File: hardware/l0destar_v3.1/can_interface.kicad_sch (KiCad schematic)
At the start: 17 parts

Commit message: update v3.1
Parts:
- removed S9J1: CAN termination jumper, Connector_PinHeader_2.54mm:PinHeader_1x02_P2.54mm_Vertical, symbol Connector:Conn_01x02_Pin
- added J1: Conn_01x02_Pin, libs:PinHeader_1x02_P2.54mm_Vertical_Tight, symbol Connector:Conn_01x02_Pin
- added S9FL1: ACT1210-101-2P-TL00, libs:ACT12101012PTL00_tight, symbol ACT1210-101-2P-TL00:ACT1210-101-2P-TL00
- S9C5: value 0603 10uF 10V 20% X7T -> 0603 10uF 10V 20% X7R
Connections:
- net CAN_H: now also S9FL1.2; no longer S9U1.7 (CANH)
- net CAN_L: now also J1.2 (Pin_2), S9FL1.3; no longer S9U1.6 (CANL)
- net at S9R3.1: now also J1.1 (Pin_1)
- new net: S9FL1.4, S9U1.6 (CANL)
- new net: S9FL1.1, S9U1.7 (CANH)
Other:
- note added: "CAN termination resistor"
- moved on the sheet: S9D1, S9R1, S9R5, S9R7

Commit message: update v3.1
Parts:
- S9C1, S9C4: Manufacturer_Name (none) -> Multicomp Pro; Manufacturer_Part_Number (none) -> MC0402B104K250CT
- S9C2, S9C3: Manufacturer_Name (none) -> Murata; Manufacturer_Part_Number (none) -> GCM1555C1H270FA16D
- S9C5: Manufacturer_Name (none) -> TDK; Manufacturer_Part_Number (none) -> C1608X7R1A106M080AT
- S9D1: Manufacturer_Name (none) -> Diotec; Manufacturer_Part_Number (none) -> NUP2105L
- S9R1, S9R2, S9R4: Manufacturer_Name (none) -> Vishay; Manufacturer_Part_Number (none) -> CRCW040210K0FKED
- S9R3: Manufacturer_Name (none) -> Multicomp Pro; Manufacturer_Part_Number (none) -> MCPAS05W2J0121T5E
- S9R5: Manufacturer_Name (none) -> Vishay; Manufacturer_Part_Number (none) -> CRCW04021K00FKED
- S9R6, S9R7: Manufacturer_Name (none) -> Multicomp; Manufacturer_Part_Number (none) -> MC00625W04021220R
- S9U2: Manufacturer_Name (none) -> Microchip; Manufacturer_Part_Number (none) -> MCP2518FD
- S9Y1: Manufacturer_Name ECS -> ECS Inc

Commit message: 3.1 updates
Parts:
- renumbered J1 to S9J1
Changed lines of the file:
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@@
 		(dnp no)
 		(fields_autoplaced yes)
-		(property "Reference" "J1"
+		(property "Reference" "S9J1"
 			(at 153.67 34.29 0)
 			(show_name no)
@@
 			(project "l0destar"
 				(path "/d9f8328e-d6fd-4b6c-867a-ed589e52ed08"
-					(reference "J1")
+					(reference "S9J1")
 					(unit 1)
 				)

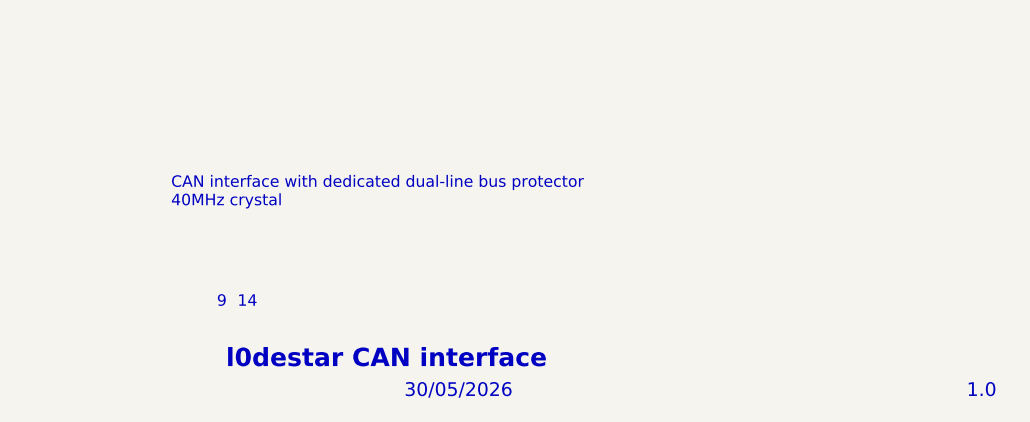
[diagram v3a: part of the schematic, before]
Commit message: update sheet annotations
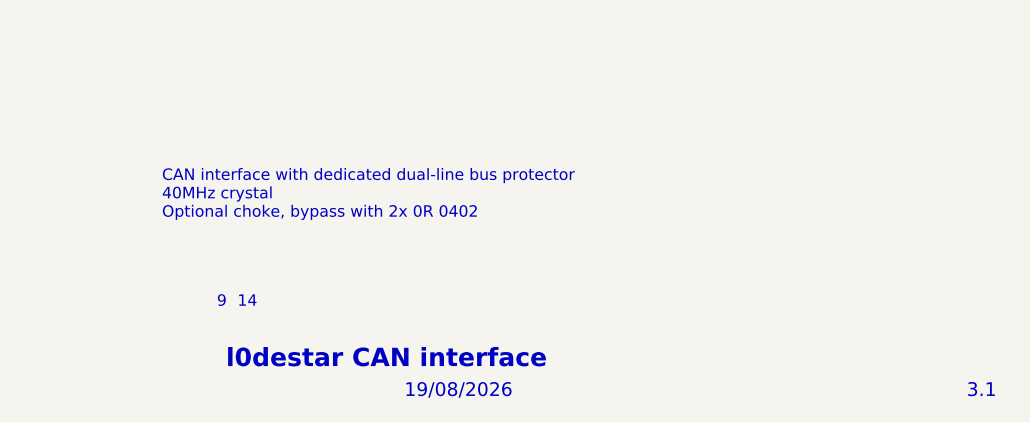
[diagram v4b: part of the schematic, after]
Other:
- note added: "19/08/2026"
- note added: "3.1"
- note added: "CAN interface with dedicated dual-line bus protector 40MHz crystal Optional choke, bypass with 2x 0R 0402"
- note removed: "1.0"
- note removed: "30/05/2026"
- note removed: "CAN interface with dedicated dual-line bus protector 40MHz crystal"
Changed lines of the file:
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@@
 	(generator_version "10.0")
 	(paper "A4")
-	(text "30/05/2026"
+	(text "19/08/2026"
 		(exclude_from_sim no)
 		(at 205.994 193.294 0)
@@
 		)
 	)
-	(text "CAN interface with dedicated dual-line bus protector\n40MHz crystal"
+	(text "CAN interface with dedicated dual-line bus protector\n40MHz crystal\nOptional choke, bypass with 2x 0R 0402"
 		(exclude_from_sim no)
-		(at 180.086 171.196 0)
+		(at 179.07 171.45 0)
 		(effects
 			(font
@@
 		)
 	)
-	(text "1.0"
+	(text "3.1"
 		(exclude_from_sim no)
 		(at 268.478 193.294 0)

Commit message: schematic<>readme discrepency fixes
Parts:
- S9C1, S9C4: value 0402 100nF 10V 10% X7R -> 0402 100nF 50V 10% X7R; Manufacturer_Name Multicomp Pro -> Murata; Manufacturer_Part_Number MC0402B104K250CT -> GRM155R71H104KE14D
- S9R2: value 0402 10K 1% -> 0402 10K 5%
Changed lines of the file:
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@@
 			)
 		)
-		(property "Value" "0402 10K 1%"
+		(property "Value" "0402 10K 5%"
 			(at 126.238 108.204 0)
 			(show_name no)
@@
 			)
 		)
-		(property "Value" "0402 100nF 10V 10% X7R"
+		(property "Value" "0402 100nF 50V 10% X7R"
 			(at 150.114 120.904 0)
 			(show_name no)
@@
 			)
 		)
-		(property "Datasheet" "https://uk.farnell.com/multicomp-pro/mc0402b104k250ct/cap-0-1-f-25v-10-x7r-0402/dp/2320759"
+		(property "Datasheet" ""
 			(at 147.32 119.38 0)
 			(hide yes)
@@
 			)
 		)
-		(property "Description" "Unpolarized capacitor"
+		(property "Description" ""
 			(at 147.32 119.38 0)
 			(hide yes)
@@
 			)
 		)
-		(property "Manufacturer_Part_Number" "MC0402B104K250CT"
+		(property "Manufacturer_Part_Number" "GRM155R71H104KE14D"
 			(at 147.32 119.38 0)
 			(hide yes)
@@
 			)
 		)
-		(property "Manufacturer_Name" "Multicomp Pro"
+		(property "Manufacturer_Name" "Murata"
 			(at 147.32 119.38 0)
 			(hide yes)
@@
 			)
 		)
-		(property "Value" "0402 100nF 10V 10% X7R"
+		(property "Value" "0402 100nF 50V 10% X7R"
 			(at 48.26 71.755 0)
 			(show_name no)
@@
 			)
 		)
-		(property "Datasheet" "https://uk.farnell.com/multicomp-pro/mc0402b104k250ct/cap-0-1-f-25v-10-x7r-0402/dp/2320759"
+		(property "Datasheet" ""
 			(at 68.58 55.88 0)
 			(hide yes)
@@
 			)
 		)
-		(property "Description" "Unpolarized capacitor"
+		(property "Description" ""
 			(at 68.58 55.88 0)
 			(hide yes)
@@
 			)
 		)
-		(property "Manufacturer_Part_Number" "MC0402B104K250CT"
+		(property "Manufacturer_Part_Number" "GRM155R71H104KE14D"
 			(at 68.58 55.88 0)
 			(hide yes)
@@
 			)
 		)
-		(property "Manufacturer_Name" "Multicomp Pro"
+		(property "Manufacturer_Name" "Murata"
 			(at 68.58 55.88 0)
 			(hide yes)
